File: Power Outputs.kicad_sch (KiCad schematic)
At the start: 30 parts, among them U4 MIC2039BYM6-TR, U5 MIC2039BYM6-TR, U6 MIC2039BYM6-TR, U7 MIC2039BYM6-TR, U8 MIC2039BYM6-TR

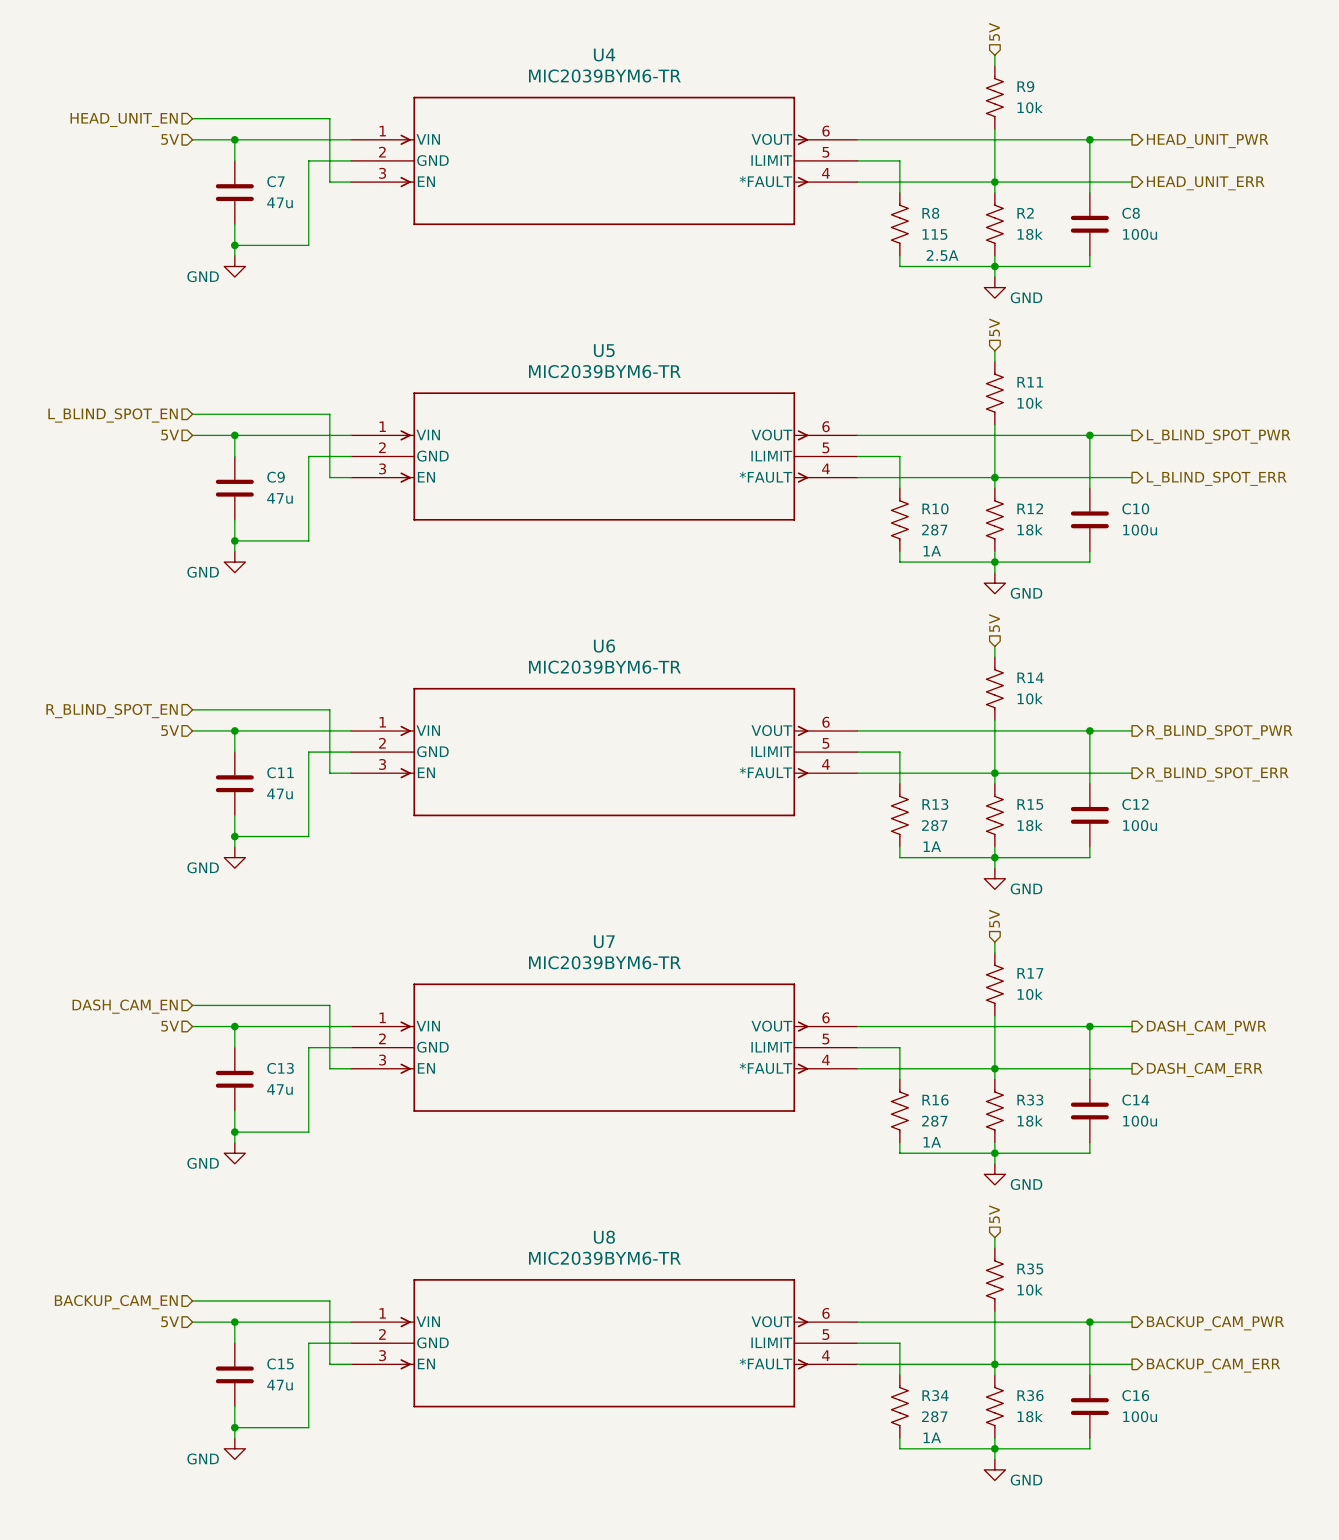
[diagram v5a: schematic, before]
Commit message: finished assigning footprints and started PCB layout
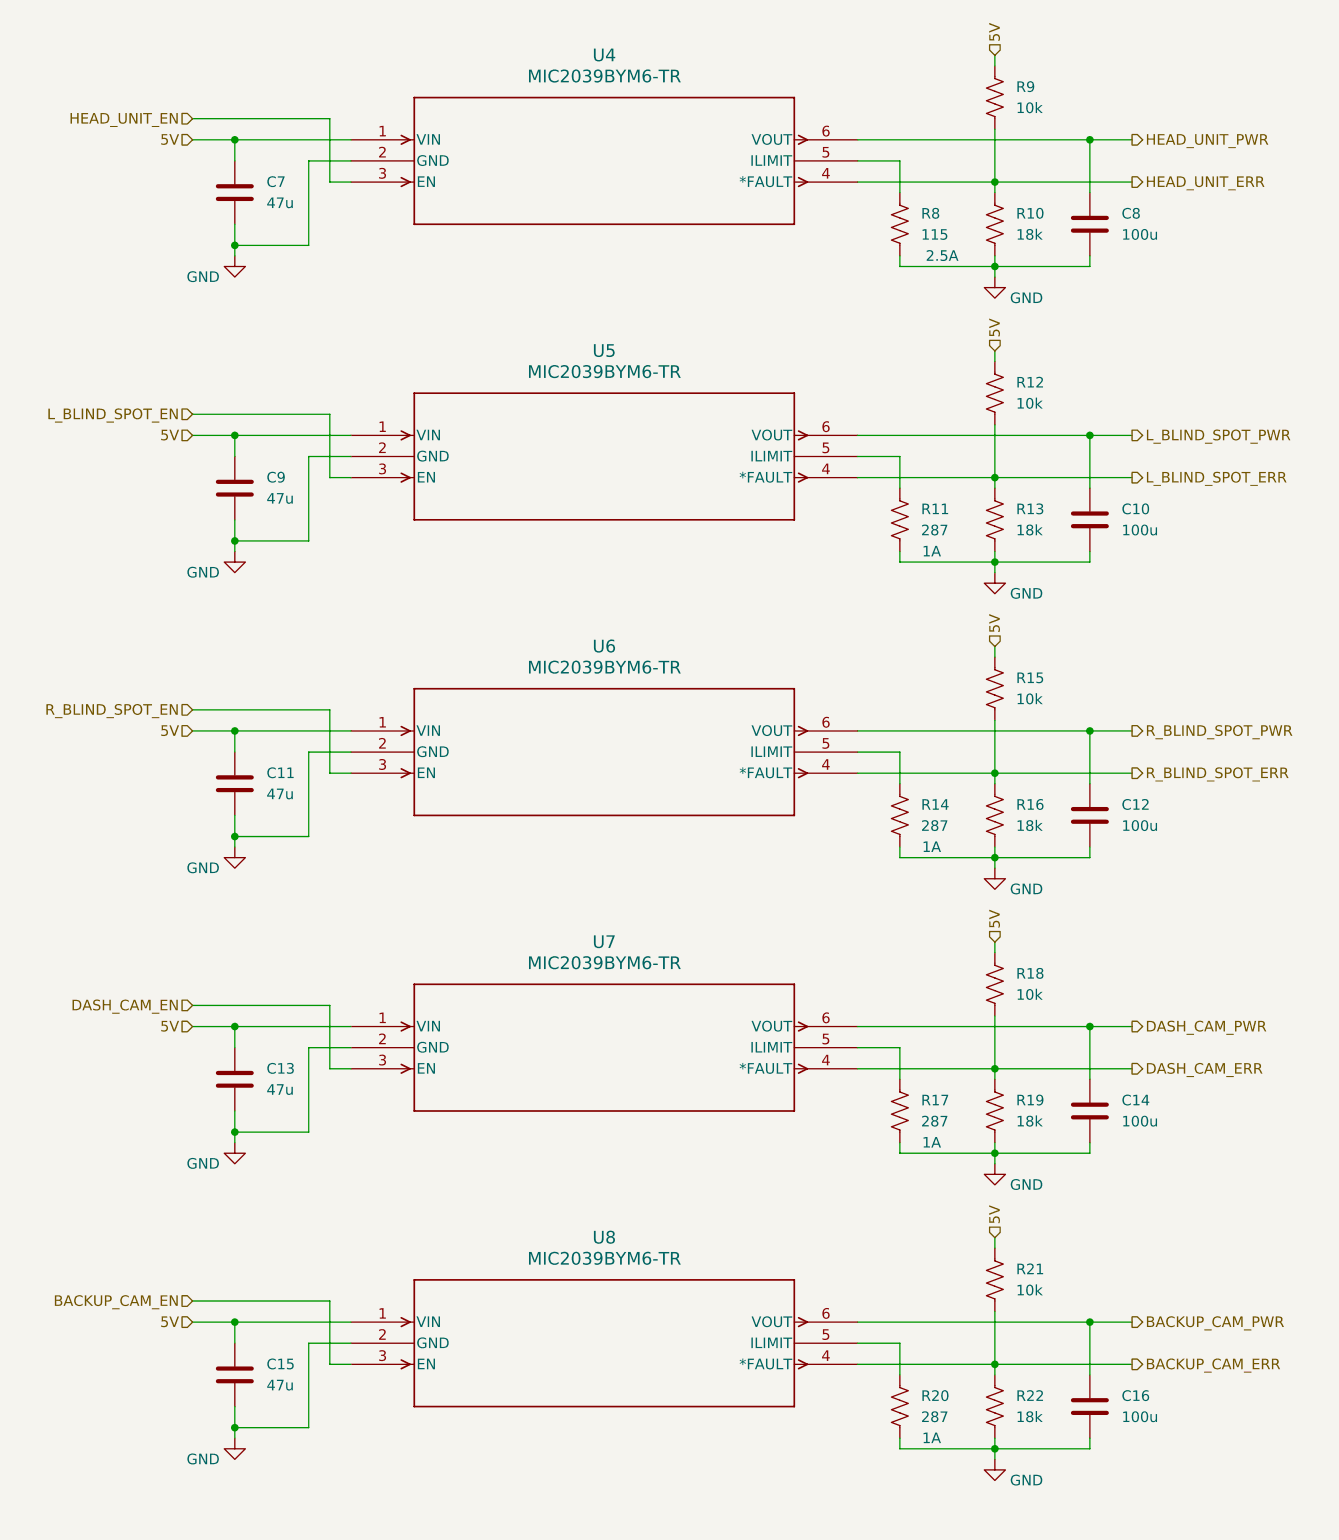
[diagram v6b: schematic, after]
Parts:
- renumbered R2 to R10, R10 to R11, R11 to R12, R12 to R13, R13 to R14, R14 to R15, R15 to R16, R16 to R17, R17 to R18, R33 to R19, R34 to R20, R35 to R21, R36 to R22
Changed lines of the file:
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@@
   (symbol (lib_id "Device:R_US") (at 139.7 147.32 0) (unit 1)
     (in_bom yes) (on_board yes) (dnp no) (fields_autoplaced)
-    (property "Reference" "R33" (at 142.24 146.05 0)
+    (property "Reference" "R19" (at 142.24 146.05 0)
       (effects (font (size 1.27 1.27)) (justify left))
     )
@@
       (project "control-module-pcb"
         (path "/4c946e98-79c2-4a2d-bd7f-2a33db8d8c91/b91ad3b4-6d59-4840-aca0-b437cb55ab0b"
-          (reference "R33") (unit 1)
+          (reference "R19") (unit 1)
         )
       )
@@
   (symbol (lib_id "Device:R_US") (at 128.27 182.88 0) (unit 1)
     (in_bom yes) (on_board yes) (dnp no)
-    (property "Reference" "R34" (at 130.81 181.61 0)
+    (property "Reference" "R20" (at 130.81 181.61 0)
       (effects (font (size 1.27 1.27)) (justify left))
     )
@@
       (project "control-module-pcb"
         (path "/4c946e98-79c2-4a2d-bd7f-2a33db8d8c91/b91ad3b4-6d59-4840-aca0-b437cb55ab0b"
-          (reference "R34") (unit 1)
+          (reference "R20") (unit 1)
         )
       )
@@
   (symbol (lib_id "Device:R_US") (at 139.7 111.76 0) (unit 1)
     (in_bom yes) (on_board yes) (dnp no) (fields_autoplaced)
-    (property "Reference" "R15" (at 142.24 110.49 0)
+    (property "Reference" "R16" (at 142.24 110.49 0)
       (effects (font (size 1.27 1.27)) (justify left))
     )
@@
       (project "control-module-pcb"
         (path "/4c946e98-79c2-4a2d-bd7f-2a33db8d8c91/b91ad3b4-6d59-4840-aca0-b437cb55ab0b"
-          (reference "R15") (unit 1)
+          (reference "R16") (unit 1)
         )
       )
@@
   (symbol (lib_id "Device:R_US") (at 128.27 147.32 0) (unit 1)
     (in_bom yes) (on_board yes) (dnp no)
-    (property "Reference" "R16" (at 130.81 146.05 0)
+    (property "Reference" "R17" (at 130.81 146.05 0)
       (effects (font (size 1.27 1.27)) (justify left))
     )
@@
       (project "control-module-pcb"
         (path "/4c946e98-79c2-4a2d-bd7f-2a33db8d8c91/b91ad3b4-6d59-4840-aca0-b437cb55ab0b"
-          (reference "R16") (unit 1)
+          (reference "R17") (unit 1)
         )
       )
@@
   (symbol (lib_id "Device:R_US") (at 139.7 76.2 0) (unit 1)
     (in_bom yes) (on_board yes) (dnp no) (fields_autoplaced)
-    (property "Reference" "R12" (at 142.24 74.93 0)
+    (property "Reference" "R13" (at 142.24 74.93 0)
       (effects (font (size 1.27 1.27)) (justify left))
     )
@@
       (project "control-module-pcb"
         (path "/4c946e98-79c2-4a2d-bd7f-2a33db8d8c91/b91ad3b4-6d59-4840-aca0-b437cb55ab0b"
-          (reference "R12") (unit 1)
+          (reference "R13") (unit 1)
         )
       )
@@
   (symbol (lib_id "Device:R_US") (at 139.7 60.96 0) (unit 1)
     (in_bom yes) (on_board yes) (dnp no) (fields_autoplaced)
-    (property "Reference" "R11" (at 142.24 59.69 0)
+    (property "Reference" "R12" (at 142.24 59.69 0)
       (effects (font (size 1.27 1.27)) (justify left))
     )
@@
       (project "control-module-pcb"
         (path "/4c946e98-79c2-4a2d-bd7f-2a33db8d8c91/b91ad3b4-6d59-4840-aca0-b437cb55ab0b"
-          (reference "R11") (unit 1)
+          (reference "R12") (unit 1)
         )
       )
@@
   (symbol (lib_id "Device:R_US") (at 139.7 132.08 0) (unit 1)
     (in_bom yes) (on_board yes) (dnp no) (fields_autoplaced)
-    (property "Reference" "R17" (at 142.24 130.81 0)
+    (property "Reference" "R18" (at 142.24 130.81 0)
       (effects (font (size 1.27 1.27)) (justify left))
     )
@@
       (project "control-module-pcb"
         (path "/4c946e98-79c2-4a2d-bd7f-2a33db8d8c91/b91ad3b4-6d59-4840-aca0-b437cb55ab0b"
-          (reference "R17") (unit 1)
+          (reference "R18") (unit 1)
         )
       )
@@
   (symbol (lib_id "Device:R_US") (at 128.27 76.2 0) (unit 1)
     (in_bom yes) (on_board yes) (dnp no)
-    (property "Reference" "R10" (at 130.81 74.93 0)
+    (property "Reference" "R11" (at 130.81 74.93 0)
       (effects (font (size 1.27 1.27)) (justify left))
     )
@@
       (project "control-module-pcb"
         (path "/4c946e98-79c2-4a2d-bd7f-2a33db8d8c91/b91ad3b4-6d59-4840-aca0-b437cb55ab0b"
-          (reference "R10") (unit 1)
+          (reference "R11") (unit 1)
         )
       )
@@
   (symbol (lib_id "Device:R_US") (at 139.7 96.52 0) (unit 1)
     (in_bom yes) (on_board yes) (dnp no) (fields_autoplaced)
-    (property "Reference" "R14" (at 142.24 95.25 0)
+    (property "Reference" "R15" (at 142.24 95.25 0)
       (effects (font (size 1.27 1.27)) (justify left))
     )
@@
       (project "control-module-pcb"
         (path "/4c946e98-79c2-4a2d-bd7f-2a33db8d8c91/b91ad3b4-6d59-4840-aca0-b437cb55ab0b"
-          (reference "R14") (unit 1)
+          (reference "R15") (unit 1)
         )
       )
@@
   (symbol (lib_id "Device:R_US") (at 139.7 40.64 0) (unit 1)
     (in_bom yes) (on_board yes) (dnp no) (fields_autoplaced)
-    (property "Reference" "R2" (at 142.24 39.37 0)
+    (property "Reference" "R10" (at 142.24 39.37 0)
       (effects (font (size 1.27 1.27)) (justify left))
     )
@@
       (project "control-module-pcb"
         (path "/4c946e98-79c2-4a2d-bd7f-2a33db8d8c91/b91ad3b4-6d59-4840-aca0-b437cb55ab0b"
-          (reference "R2") (unit 1)
+          (reference "R10") (unit 1)
         )
       )
@@
   (symbol (lib_id "Device:R_US") (at 128.27 111.76 0) (unit 1)
     (in_bom yes) (on_board yes) (dnp no)
-    (property "Reference" "R13" (at 130.81 110.49 0)
+    (property "Reference" "R14" (at 130.81 110.49 0)
       (effects (font (size 1.27 1.27)) (justify left))
     )
@@
       (project "control-module-pcb"
         (path "/4c946e98-79c2-4a2d-bd7f-2a33db8d8c91/b91ad3b4-6d59-4840-aca0-b437cb55ab0b"
-          (reference "R13") (unit 1)
+          (reference "R14") (unit 1)
         )
       )
@@
   (symbol (lib_id "Device:R_US") (at 139.7 182.88 0) (unit 1)
     (in_bom yes) (on_board yes) (dnp no) (fields_autoplaced)
-    (property "Reference" "R36" (at 142.24 181.61 0)
+    (property "Reference" "R22" (at 142.24 181.61 0)
       (effects (font (size 1.27 1.27)) (justify left))
     )
@@
       (project "control-module-pcb"
         (path "/4c946e98-79c2-4a2d-bd7f-2a33db8d8c91/b91ad3b4-6d59-4840-aca0-b437cb55ab0b"
-          (reference "R36") (unit 1)
+          (reference "R22") (unit 1)
         )
       )
@@
   (symbol (lib_id "Device:R_US") (at 139.7 167.64 0) (unit 1)
     (in_bom yes) (on_board yes) (dnp no) (fields_autoplaced)
-    (property "Reference" "R35" (at 142.24 166.37 0)
+    (property "Reference" "R21" (at 142.24 166.37 0)
       (effects (font (size 1.27 1.27)) (justify left))
     )
@@
       (project "control-module-pcb"
         (path "/4c946e98-79c2-4a2d-bd7f-2a33db8d8c91/b91ad3b4-6d59-4840-aca0-b437cb55ab0b"
-          (reference "R35") (unit 1)
-        )
-      )
+          (reference "R21") (unit 1)
+        )
+      )

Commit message: made a few adjustments and generated gerbers
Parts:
- R8: value 115 -> 145; Current Limit 2.5A -> 2A
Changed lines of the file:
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@@
       (effects (font (size 1.27 1.27)) (justify left))
     )
-    (property "Value" "115" (at 130.81 41.91 0)
+    (property "Value" "145" (at 130.81 41.91 0)
       (effects (font (size 1.27 1.27)) (justify left))
     )
@@
       (effects (font (size 1.27 1.27)) hide)
     )
-    (property "Current Limit" "2.5A" (at 133.35 44.45 0)
+    (property "Current Limit" "2A" (at 132.08 44.45 0)
       (effects (font (size 1.27 1.27)))
     )
